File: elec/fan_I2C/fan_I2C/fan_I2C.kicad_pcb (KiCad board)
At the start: 2 copper layers, 83 x 160 mm, 2 parts, among them J101 DB9_Female_MountingHoles, J102 DB25_Female_MountingHoles

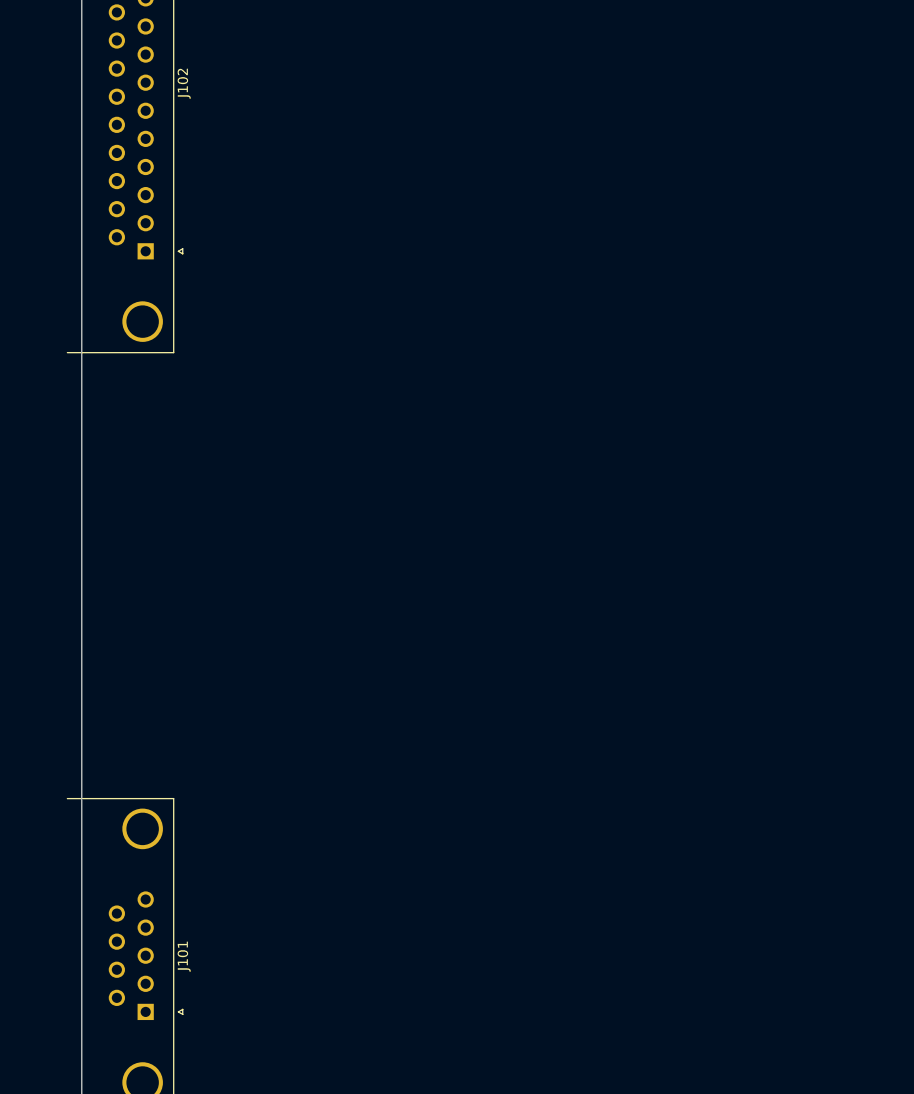
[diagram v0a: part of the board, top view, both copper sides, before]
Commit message: Add Connectors RJ12 and JST.
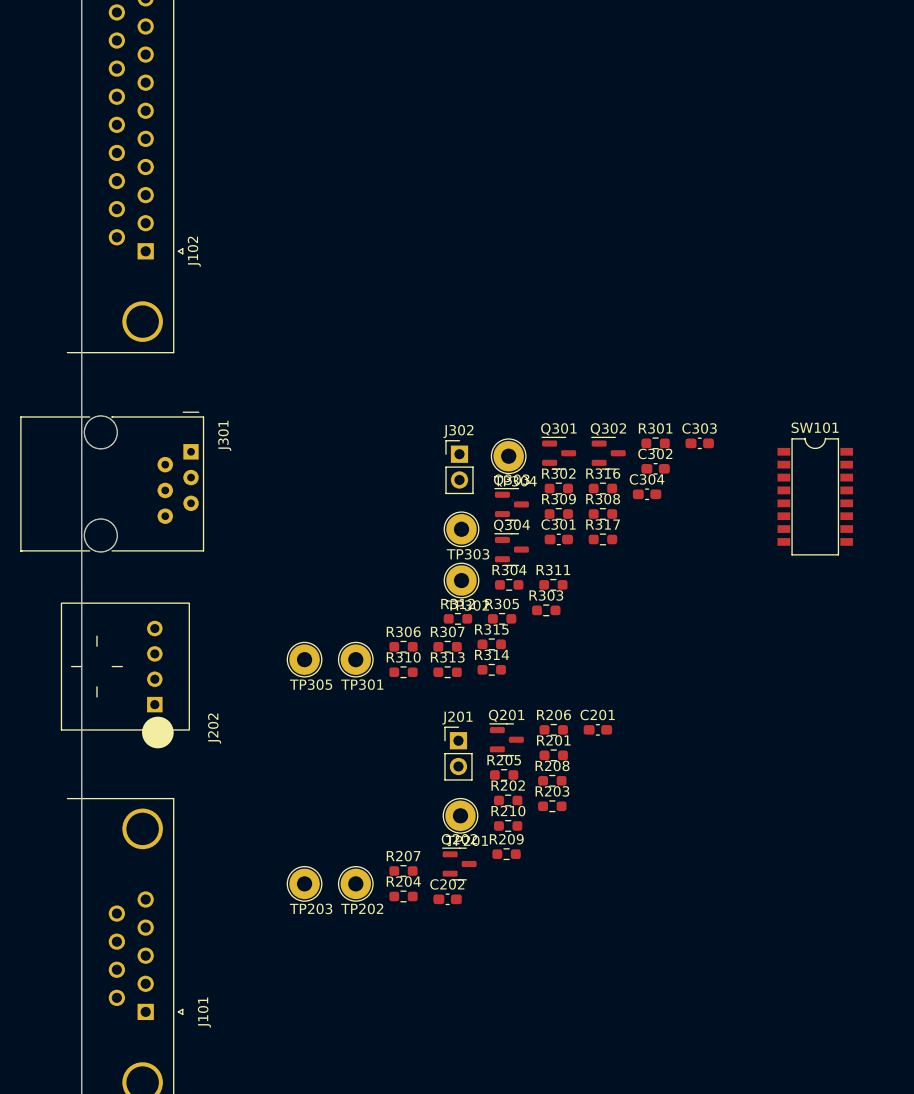
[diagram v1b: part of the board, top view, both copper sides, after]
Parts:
- added C201: 39PF, Capacitor_SMD:C_0603_1608Metric_Pad1.08x0.95mm_HandSolder, F.Cu at (139.9, 125.2)
- added C202: 39PF, Capacitor_SMD:C_0603_1608Metric_Pad1.08x0.95mm_HandSolder, F.Cu at (125.1, 141.9)
- added C301: 39PF, Capacitor_SMD:C_0603_1608Metric_Pad1.08x0.95mm_HandSolder, F.Cu at (136.0, 106.5)
- added C302: 39PF, Capacitor_SMD:C_0603_1608Metric_Pad1.08x0.95mm_HandSolder, F.Cu at (145.6, 99.5)
- added C303: 39PF, Capacitor_SMD:C_0603_1608Metric_Pad1.08x0.95mm_HandSolder, F.Cu at (149.9, 97.0)
- added C304: 39PF, Capacitor_SMD:C_0603_1608Metric_Pad1.08x0.95mm_HandSolder, F.Cu at (144.7, 102.0)
- added J201: 0.100_2Pin, Connector_PinHeader_2.54mm:PinHeader_1x02_P2.54mm_Vertical, F.Cu at (126.1, 126.3)
- added J202: S04B-XASK-1(LF)(SN), PubInv_PCB:S04B-XASK-1(LF)(SN), F.Cu at (87.0, 119.0)
- added J301: RJ12_6P6C_HORZ, PubInv_PCB:RJ12_Amphenol_54601, F.Cu at (99.8, 97.8)
- added J302: 0.100_2Pin, Connector_PinHeader_2.54mm:PinHeader_1x02_P2.54mm_Vertical, F.Cu at (126.2, 98.1)
- added Q201: BSS138, Package_TO_SOT_SMD:SOT-23, F.Cu at (130.9, 126.2)
- added Q202: BSS138, Package_TO_SOT_SMD:SOT-23, F.Cu at (126.2, 138.5)
- added Q301: BSS138, Package_TO_SOT_SMD:SOT-23, F.Cu at (136.1, 98.0)
- added Q302: BSS138, Package_TO_SOT_SMD:SOT-23, F.Cu at (140.9, 98.0)
- added Q303: BSS138, Package_TO_SOT_SMD:SOT-23, F.Cu at (131.4, 103.0)
- added Q304: BSS138, Package_TO_SOT_SMD:SOT-23, F.Cu at (131.4, 107.5)
- added R201: 1R, Resistor_SMD:R_0603_1608Metric_Pad0.98x0.95mm_HandSolder, F.Cu at (135.5, 127.8)
- added R202: 10K, Resistor_SMD:R_0603_1608Metric_Pad0.98x0.95mm_HandSolder, F.Cu at (131.0, 132.2)
- added R203: 10K, Resistor_SMD:R_0603_1608Metric_Pad0.98x0.95mm_HandSolder, F.Cu at (135.4, 132.8)
- added R204: 10K, Resistor_SMD:R_0603_1608Metric_Pad0.98x0.95mm_HandSolder, F.Cu at (120.7, 141.7)
- added R205: 10K, Resistor_SMD:R_0603_1608Metric_Pad0.98x0.95mm_HandSolder, F.Cu at (130.6, 129.7)
- added R206: 39R, Resistor_SMD:R_0603_1608Metric_Pad0.98x0.95mm_HandSolder, F.Cu at (135.5, 125.2)
- added R207: 39R, Resistor_SMD:R_0603_1608Metric_Pad0.98x0.95mm_HandSolder, F.Cu at (120.7, 139.2)
- added R208: 1R, Resistor_SMD:R_0603_1608Metric_Pad0.98x0.95mm_HandSolder, F.Cu at (135.4, 130.3)
- added R209: DNI, Resistor_SMD:R_0603_1608Metric_Pad0.98x0.95mm_HandSolder, F.Cu at (130.9, 137.5)
- added R210: DNI, Resistor_SMD:R_0603_1608Metric_Pad0.98x0.95mm_HandSolder, F.Cu at (131.0, 134.7)
- added R301: 1R, Resistor_SMD:R_0603_1608Metric_Pad0.98x0.95mm_HandSolder, F.Cu at (145.6, 97.0)
- added R302: 1R, Resistor_SMD:R_0603_1608Metric_Pad0.98x0.95mm_HandSolder, F.Cu at (136.0, 101.5)
- added R303: DNI, Resistor_SMD:R_0603_1608Metric_Pad0.98x0.95mm_HandSolder, F.Cu at (134.8, 113.5)
- added R304: DNI, Resistor_SMD:R_0603_1608Metric_Pad0.98x0.95mm_HandSolder, F.Cu at (131.1, 111.0)
- added R305: DNI, Resistor_SMD:R_0603_1608Metric_Pad0.98x0.95mm_HandSolder, F.Cu at (130.4, 114.3)
- added R306: 1K, Resistor_SMD:R_0603_1608Metric_Pad0.98x0.95mm_HandSolder, F.Cu at (120.7, 117.0)
- added R307: DNI, Resistor_SMD:R_0603_1608Metric_Pad0.98x0.95mm_HandSolder, F.Cu at (125.1, 117.0)
- added R308: 10K, Resistor_SMD:R_0603_1608Metric_Pad0.98x0.95mm_HandSolder, F.Cu at (140.4, 104.0)
- added R309: 1K, Resistor_SMD:R_0603_1608Metric_Pad0.98x0.95mm_HandSolder, F.Cu at (136.0, 104.0)
- added R310: 1K, Resistor_SMD:R_0603_1608Metric_Pad0.98x0.95mm_HandSolder, F.Cu at (120.7, 119.6)
- added R311: 1R, Resistor_SMD:R_0603_1608Metric_Pad0.98x0.95mm_HandSolder, F.Cu at (135.5, 111.0)
- added R312: DNI, Resistor_SMD:R_0603_1608Metric_Pad0.98x0.95mm_HandSolder, F.Cu at (126.1, 114.3)
- added R313: 10K, Resistor_SMD:R_0603_1608Metric_Pad0.98x0.95mm_HandSolder, F.Cu at (125.1, 119.6)
- added R314: 1K, Resistor_SMD:R_0603_1608Metric_Pad0.98x0.95mm_HandSolder, F.Cu at (129.4, 119.3)
- added R315: DNI, Resistor_SMD:R_0603_1608Metric_Pad0.98x0.95mm_HandSolder, F.Cu at (129.4, 116.8)
- added R316: 10K, Resistor_SMD:R_0603_1608Metric_Pad0.98x0.95mm_HandSolder, F.Cu at (140.4, 101.5)
- added R317: 10K, Resistor_SMD:R_0603_1608Metric_Pad0.98x0.95mm_HandSolder, F.Cu at (140.4, 106.5)
- added SW101: SW_DIP_x08, PubInv_PCB:SMDIP-16_L11.39_W6.7mm, F.Cu at (161.3, 102.3)
- added TP201: I2C_VCC, TestPoint:TestPoint_Loop_D2.54mm_Drill1.5mm_Beaded, F.Cu at (126.3, 133.7)
- added TP202: SCL_5V, TestPoint:TestPoint_Loop_D2.54mm_Drill1.5mm_Beaded, F.Cu at (116.0, 140.4)
- added TP203: SDA_5V, TestPoint:TestPoint_Loop_D2.54mm_Drill1.5mm_Beaded, F.Cu at (111.0, 140.4)
- added TP301: ControllerVCC, TestPoint:TestPoint_Loop_D2.54mm_Drill1.5mm_Beaded, F.Cu at (116.0, 118.3)
- added TP302: CPIO, TestPoint:TestPoint_Loop_D2.54mm_Drill1.5mm_Beaded, F.Cu at (126.4, 110.5)
- added TP303: SCK, TestPoint:TestPoint_Loop_D2.54mm_Drill1.5mm_Beaded, F.Cu at (126.4, 105.5)
- added TP304: COPI, TestPoint:TestPoint_Loop_D2.54mm_Drill1.5mm_Beaded, F.Cu at (131.1, 98.3)
- added TP305: nCS, TestPoint:TestPoint_Loop_D2.54mm_Drill1.5mm_Beaded, F.Cu at (111.0, 118.3)
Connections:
- J101 pad 2: unconnected-(J101-Pad2) -> /I2C_LevelShift/SCL_5V
- J101 pad 4: unconnected-(J101-Pad4) -> /I2C_LevelShift/SDA_5V

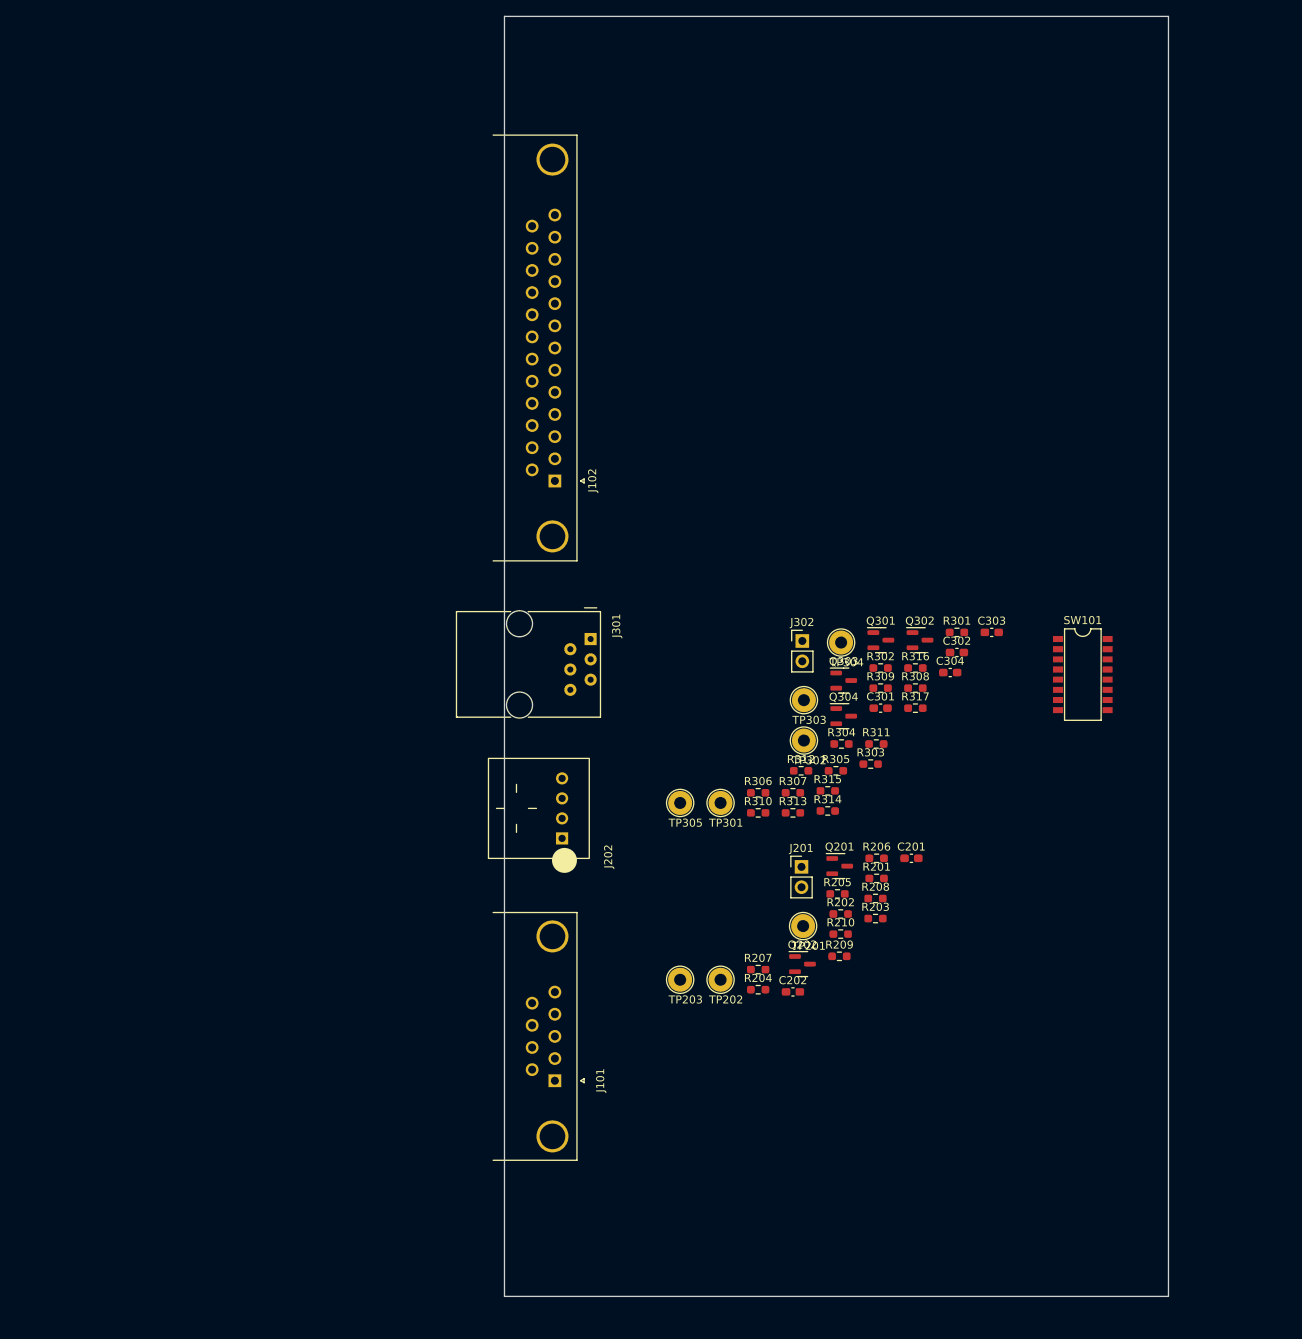
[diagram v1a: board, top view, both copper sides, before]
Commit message: Add Connectors like Roberts Fritzing.
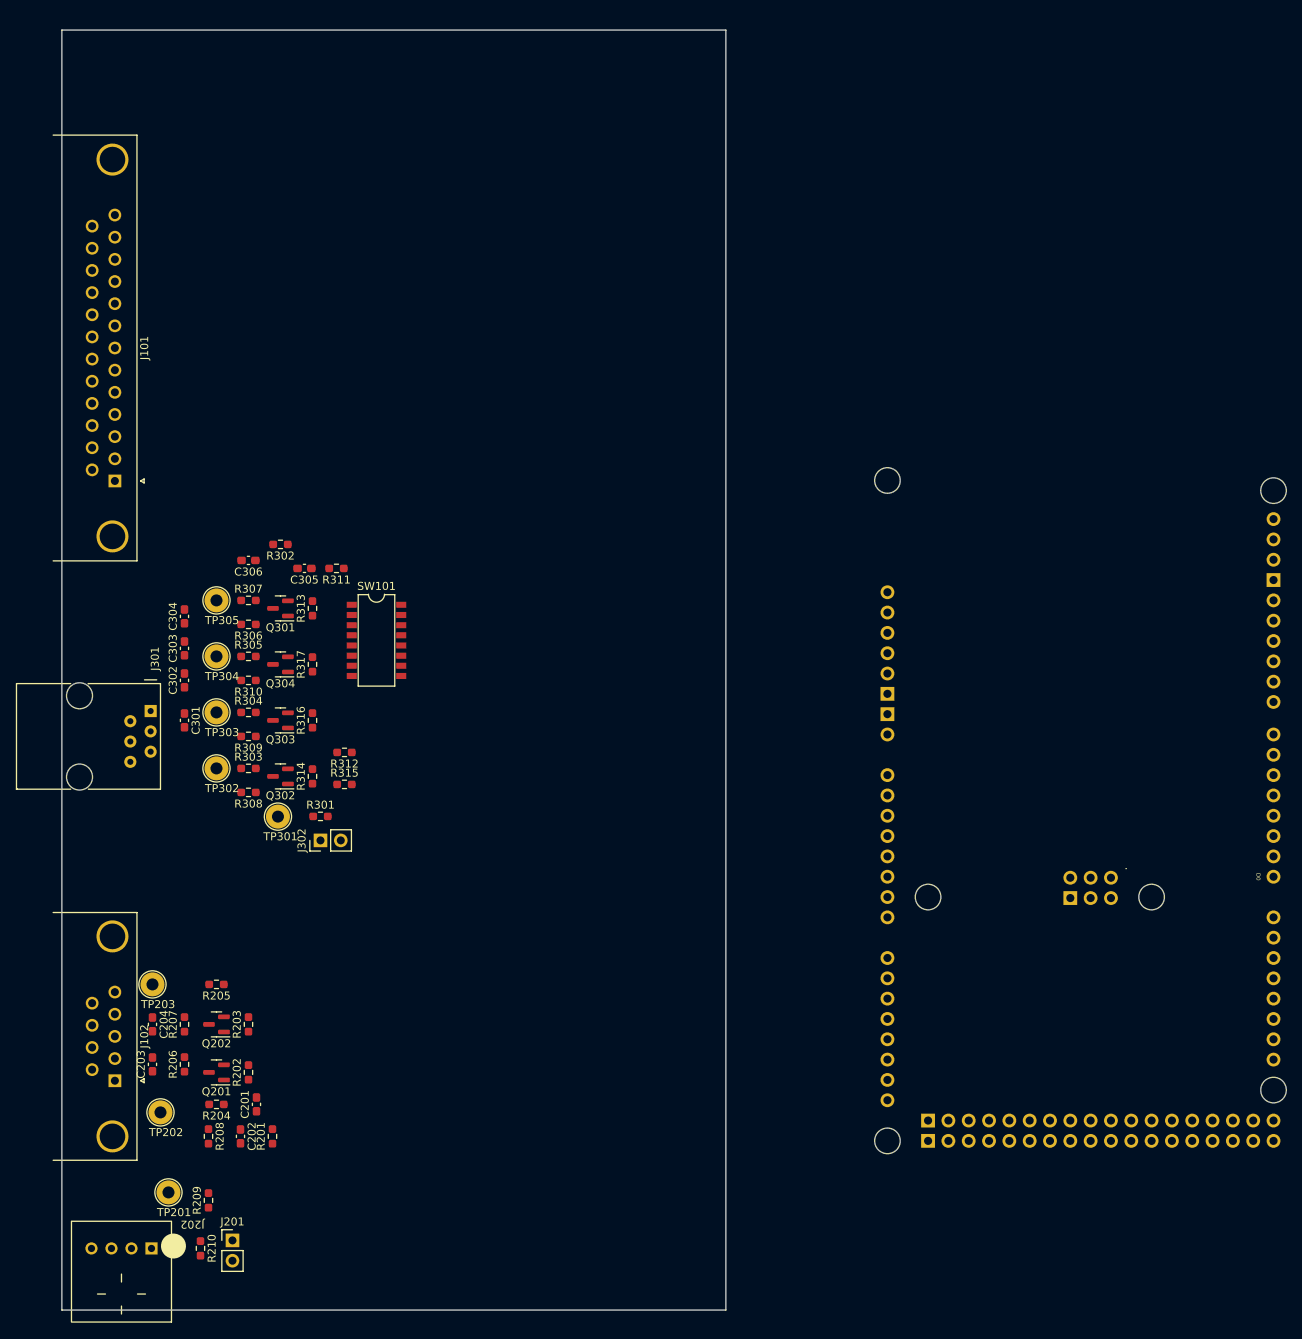
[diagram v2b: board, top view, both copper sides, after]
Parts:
- added C203: 39PF, Capacitor_SMD:C_0603_1608Metric_Pad1.08x0.95mm_HandSolder, F.Cu at (45.0, 151.0)
- added C204: 39PF, Capacitor_SMD:C_0603_1608Metric_Pad1.08x0.95mm_HandSolder, F.Cu at (45.0, 146.0)
- added C305: 1uF, Capacitor_SMD:C_0603_1608Metric_Pad1.08x0.95mm_HandSolder, F.Cu at (64.0, 89.0)
- added C306: 1uF, Capacitor_SMD:C_0603_1608Metric_Pad1.08x0.95mm_HandSolder, F.Cu at (57.0, 88.0)
- added XA101: Arduino_Due_Shield, arduino-library:Arduino_Due_Shield, F.Cu at (134.3, 64.0)
- C201, C202: value 39PF -> 1uF
- J101: value DB9_Female_MountingHoles -> DB25_Female_MountingHoles; footprint Connector_Dsub:DSUB-9_Female_Horizontal_P2.77x2.84mm_EdgePinOffset4.94mm_Housed_MountingHolesOffset7.48mm -> Connector_Dsub:DSUB-25_Female_Horizontal_P2.77x2.84mm_EdgePinOffset4.94mm_Housed_MountingHolesOffset7.48mm
- J102: value DB25_Female_MountingHoles -> DB9_Female_MountingHoles; footprint Connector_Dsub:DSUB-25_Female_Horizontal_P2.77x2.84mm_EdgePinOffset4.94mm_Housed_MountingHolesOffset7.48mm -> Connector_Dsub:DSUB-9_Female_Horizontal_P2.77x2.84mm_EdgePinOffset4.94mm_Housed_MountingHolesOffset7.48mm
- moved C303 100.9 mm to (49.0, 99.0), turned to 90 degrees
- moved C302 96.6 mm to (49.0, 103.0), turned to 90 degrees
- moved C304 96.0 mm to (49.0, 95.0), turned to 90 degrees
- moved J101 93.0 mm to (40.3, 78.1)
- moved J102 93.0 mm to (40.3, 153.0)
- moved R206 90.3 mm to (49.0, 151.0), turned to 90 degrees
- moved R210 89.2 mm to (51.0, 174.0), turned to -90 degrees
- moved R208 88.5 mm to (52.0, 160.0), turned to -90 degrees
- moved SW101 88.4 mm to (73.0, 98.0)
- moved C201 87.5 mm to (58.0, 156.0), turned to 90 degrees
- moved C301 87.0 mm to (49.0, 108.0), turned to -90 degrees
- moved TP201 86.0 mm to (47.0, 167.0)
- moved J201 85.1 mm to (55.0, 173.0)
- moved R209 84.6 mm to (52.0, 168.0), turned to 90 degrees
- moved R308 84.4 mm to (57.0, 117.0), turned to 180 degrees
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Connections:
- net /I2C_LevelShift/SCL_3.3V renamed SCL
- net /I2C_LevelShift/SDA_3.3V renamed SDA
- net /SPI_ControllerLevel_Shifter/CIPO_3V3 renamed CIPO
- net /SPI_ControllerLevel_Shifter/COPI_3V3 renamed COPI
- net /SPI_ControllerLevel_Shifter/SCK_3V3 renamed SPI_SCK
- C201 pad 1: /I2C_LevelShift/SCL_5V -> /I2C_LevelShift/+3V3Local
- C202 pad 1: /I2C_LevelShift/SDA_5V -> /I2C_LevelShift/+5VLocal
- J101 pad 2: /I2C_LevelShift/SCL_5V -> unconnected-(J101-Pad2)
- J101 pad 3: GND -> unconnected-(J101-Pad3)
- J101 pad 4: /I2C_LevelShift/SDA_5V -> unconnected-(J101-Pad4)
- J101 pad 6: GND -> unconnected-(J101-Pad6)
- J101 pad 7: GND -> unconnected-(J101-Pad7)
- J101 pad 8: GND -> unconnected-(J101-Pad8)
- J101 pad 9: GND -> unconnected-(J101-Pad9)
- J102 pad 2: unconnected-(J102-Pad2) -> /I2C_LevelShift/SCL_5V
- J102 pad 3: unconnected-(J102-Pad3) -> GND
- J102 pad 4: unconnected-(J102-Pad4) -> /I2C_LevelShift/SDA_5V
- J102 pad 6: unconnected-(J102-Pad6) -> GND
- J102 pad 7: unconnected-(J102-Pad7) -> GND
- J102 pad 8: unconnected-(J102-Pad8) -> GND
- J102 pad 9: unconnected-(J102-Pad9) -> GND
